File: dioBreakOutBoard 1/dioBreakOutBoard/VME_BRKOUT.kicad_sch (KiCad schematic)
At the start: 2 parts, among them J11 56509455, J12 56509455

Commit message: C:\Users\khernandez\KiCad\KiCad-Projects# Please enter the commit message for your changes. Lines starting
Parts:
- removed J12: 56509455, Connectors_kmh:56509455, symbol 09031646922:09031646922
- added J3: 5205869-2, Connectors_kmh:52058692, symbol 5205869-2:5205869-2
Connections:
- net DIO_0: now also J3.1
- net DIO_1: now also J3.2
- net DIO_10: now also J3.11
- net DIO_11: now also J3.12
- net DIO_12: now also J3.13
- net DIO_13: now also J3.14
- net DIO_14: now also J3.15
- net DIO_15: now also J3.16
- net DIO_16: now also J3.17
- net DIO_17: now also J3.18
- net DIO_18: now also J3.19
- net DIO_19: now also J3.20
- net DIO_2: now also J3.3
- net DIO_20: now also J3.21
- net DIO_21: now also J3.22
- net DIO_22: now also J3.23
- net DIO_23: now also J3.24
- net DIO_24: now also J3.25
- net DIO_25: now also J3.26
- net DIO_26: now also J3.27
- net DIO_27: now also J3.28
- net DIO_28: now also J3.32
- net DIO_29: now also J3.36
- net DIO_3: now also J3.4
- net DIO_30: now also J3.40
- net DIO_31: now also J3.44
- net DIO_32: now also J11.A1; no longer J11.A32
- net DIO_33: now also J11.A2; no longer J11.A31
- net DIO_34: now also J11.A3; no longer J11.A30
- net DIO_35: now also J11.A4; no longer J11.A29
- net DIO_36: now also J11.A5; no longer J11.A28
- net DIO_37: now also J11.A6; no longer J11.A27
- net DIO_38: now also J11.A7; no longer J11.A26
- net DIO_39: now also J11.A8; no longer J11.A25
- net DIO_4: now also J3.5
- net DIO_40: now also J11.A9; no longer J11.A24
- net DIO_41: now also J11.A10; no longer J11.A23
- net DIO_42: now also J11.A11; no longer J11.A22
- net DIO_43: now also J11.A12; no longer J11.A21
- net DIO_44: now also J11.A13; no longer J11.A20
- net DIO_45: now also J11.A14; no longer J11.A19
- net DIO_46: now also J11.A15; no longer J11.A18
- net DIO_47: now also J11.A16; no longer J11.A17
- net DIO_48: now also J11.A17; no longer J11.A16
- net DIO_49: now also J11.A18; no longer J11.A15
- net DIO_5: now also J3.6
- net DIO_50: now also J11.A19; no longer J11.A14
- net DIO_51: now also J11.A20; no longer J11.A13
- net DIO_52: now also J11.A21; no longer J11.A12
- net DIO_53: now also J11.A22; no longer J11.A11
- net DIO_54: now also J11.A23; no longer J11.A10
- net DIO_55: now also J11.A24; no longer J11.A9
- net DIO_56: now also J11.A25; no longer J11.A8
- net DIO_57: now also J11.A26; no longer J11.A7
- net DIO_58: now also J11.A27; no longer J11.A6
- net DIO_59: now also J11.A28; no longer J11.A5
- net DIO_6: now also J3.7
- net DIO_60: now also J11.A29; no longer J11.A4
- net DIO_61: now also J11.A30; no longer J11.A3
- net DIO_62: now also J11.A31; no longer J11.A2
- net DIO_63: now also J11.A32; no longer J11.A1
- net DIO_7: now also J3.8
- net DIO_8: now also J3.9
- net DIO_9: now also J3.10
- net GND: now also J3.29, J3.30, J3.31, J3.33, J3.34, J3.35, J3.37, J3.38, J3.39, J3.41, J3.42, J3.43, J3.45, J3.46, J3.47, J3.48, J3.49, J3.50, J3.MH1, J3.MH2, J3.MH3, J3.MH4

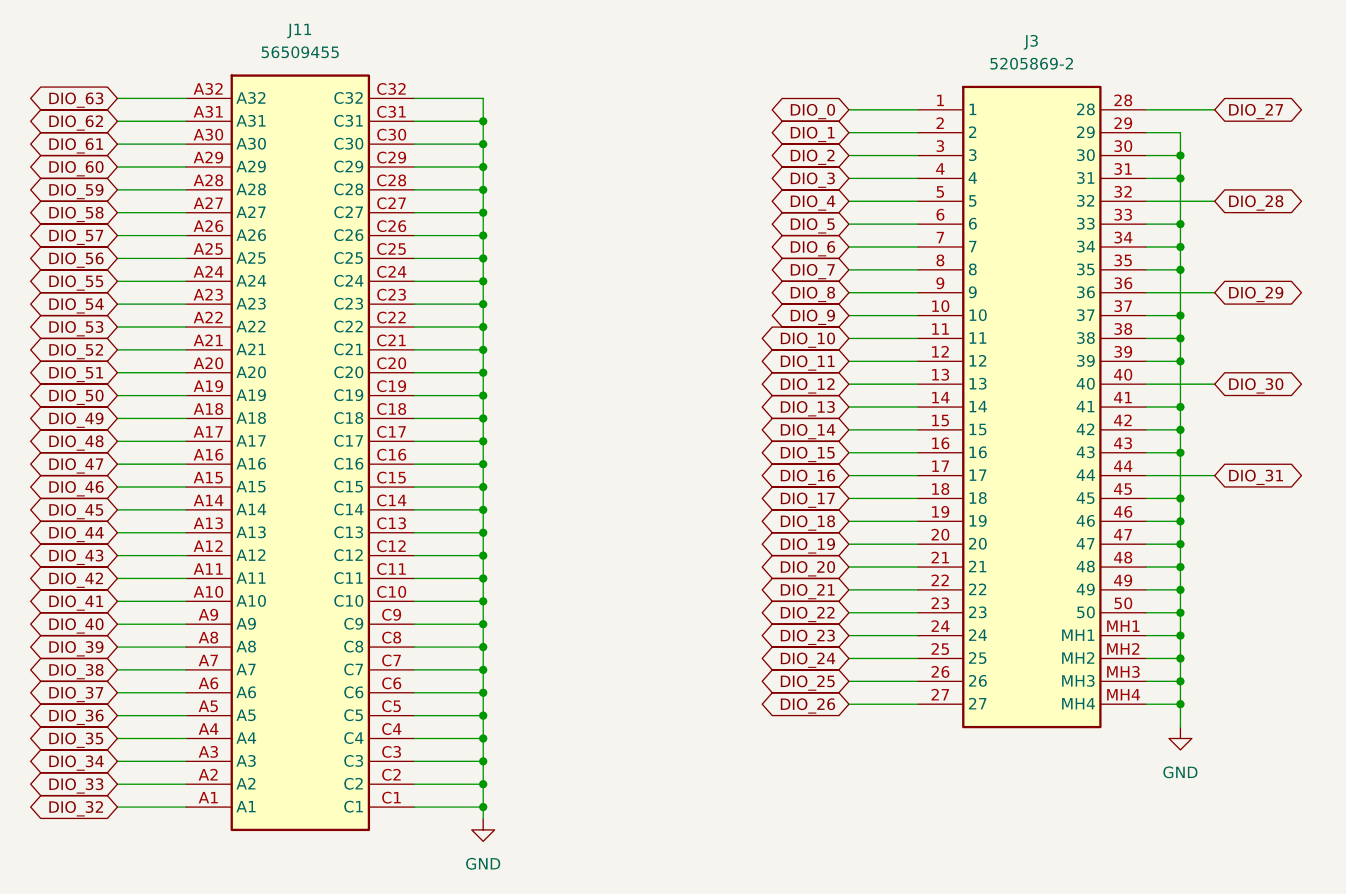
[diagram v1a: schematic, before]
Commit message: added 2 bit buffers, which replace the previous 8 bit buffers
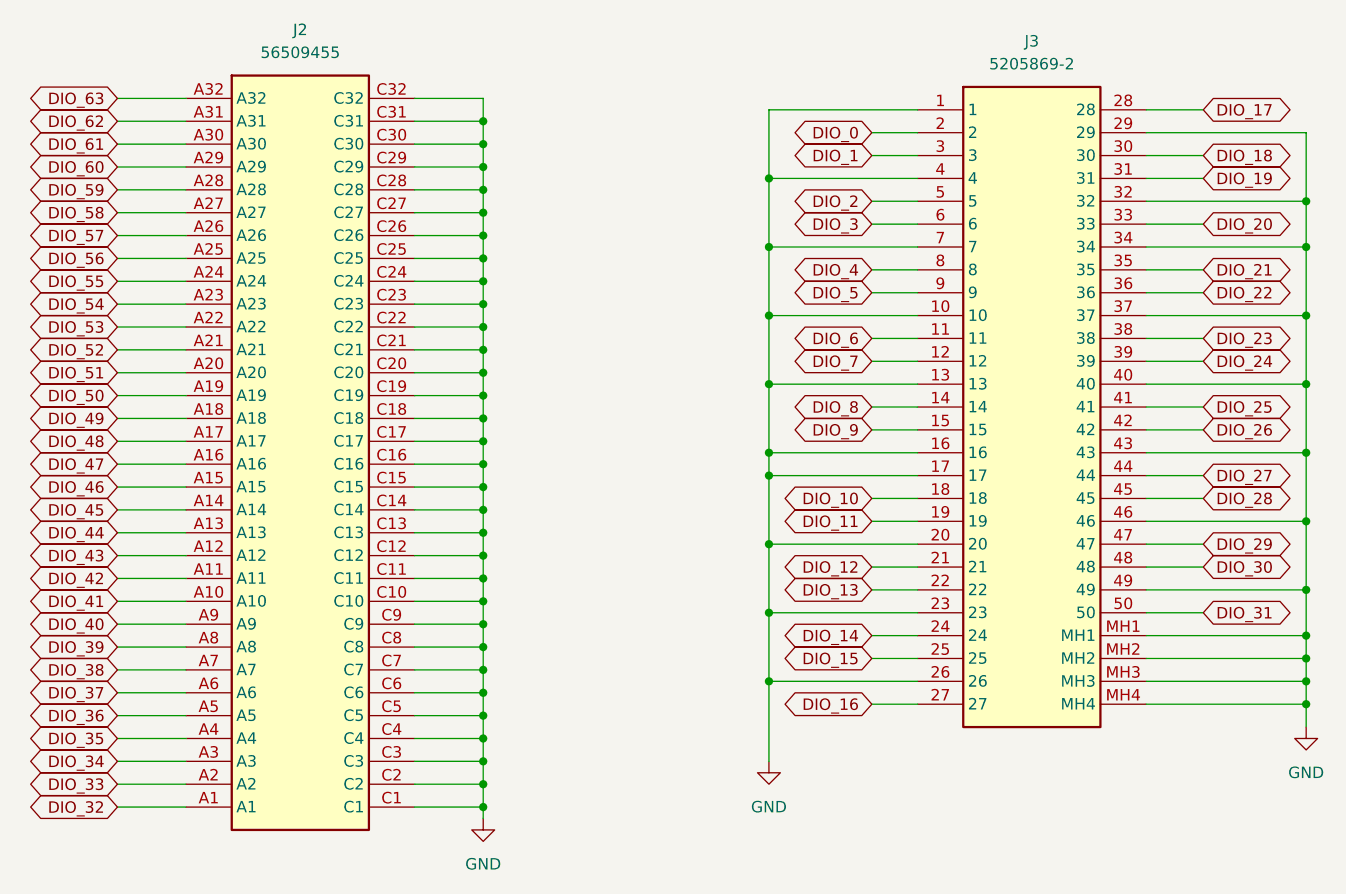
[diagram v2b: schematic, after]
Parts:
- renumbered J11 to J2
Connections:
- net DIO_0: now also J3.2; no longer J3.1
- net DIO_1: now also J3.3; no longer J3.2
- net DIO_10: now also J3.18; no longer J3.11
- net DIO_11: now also J3.19; no longer J3.12
- net DIO_12: now also J3.21; no longer J3.13
- net DIO_13: now also J3.22; no longer J3.14
- net DIO_14: now also J3.24; no longer J3.15
- net DIO_15: now also J3.25; no longer J3.16
- net DIO_16: now also J3.27; no longer J3.17
- net DIO_17: now also J3.28; no longer J3.18
- net DIO_18: now also J3.30; no longer J3.19
- net DIO_19: now also J3.31; no longer J3.20
- net DIO_2: now also J3.5; no longer J3.3
- net DIO_20: now also J3.33; no longer J3.21
- net DIO_21: now also J3.35; no longer J3.22
- net DIO_22: now also J3.36; no longer J3.23
- net DIO_23: now also J3.38; no longer J3.24
- net DIO_24: now also J3.39; no longer J3.25
- net DIO_25: now also J3.41; no longer J3.26
- net DIO_26: now also J3.42; no longer J3.27
- net DIO_27: now also J3.44; no longer J3.28
- net DIO_28: now also J3.45; no longer J3.32
- net DIO_29: now also J3.47; no longer J3.36
- net DIO_3: now also J3.6; no longer J3.4
- net DIO_30: now also J3.48; no longer J3.40
- net DIO_31: now also J3.50; no longer J3.44
- net DIO_4: now also J3.8; no longer J3.5
- net DIO_5: now also J3.9; no longer J3.6
- net DIO_6: now also J3.11; no longer J3.7
- net DIO_7: now also J3.12; no longer J3.8
- net DIO_8: now also J3.14; no longer J3.9
- net DIO_9: now also J3.15; no longer J3.10
- net GND: now also J3.1, J3.10, J3.13, J3.16, J3.17, J3.20, J3.23, J3.26, J3.32, J3.4, J3.40, J3.7; no longer J3.30, J3.31, J3.33, J3.35, J3.38, J3.39, J3.41, J3.42, J3.45, J3.47, J3.48, J3.50
